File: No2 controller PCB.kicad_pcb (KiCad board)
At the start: 2 copper layers, 155 x 70 mm, 11 parts, among them SW1 SW_Push, SW2 SW_Push, U1 ProMicro

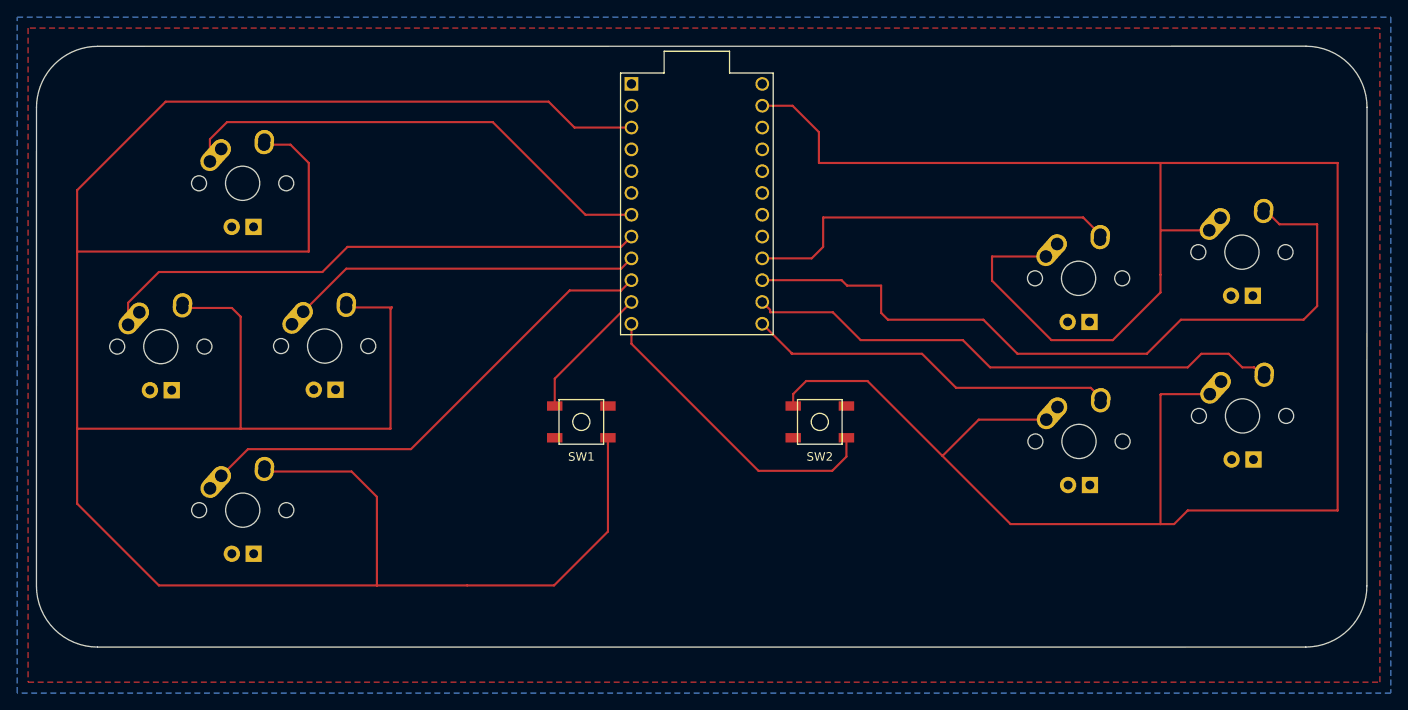
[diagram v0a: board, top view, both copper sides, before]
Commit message: added silkscreen, submitted to JLC
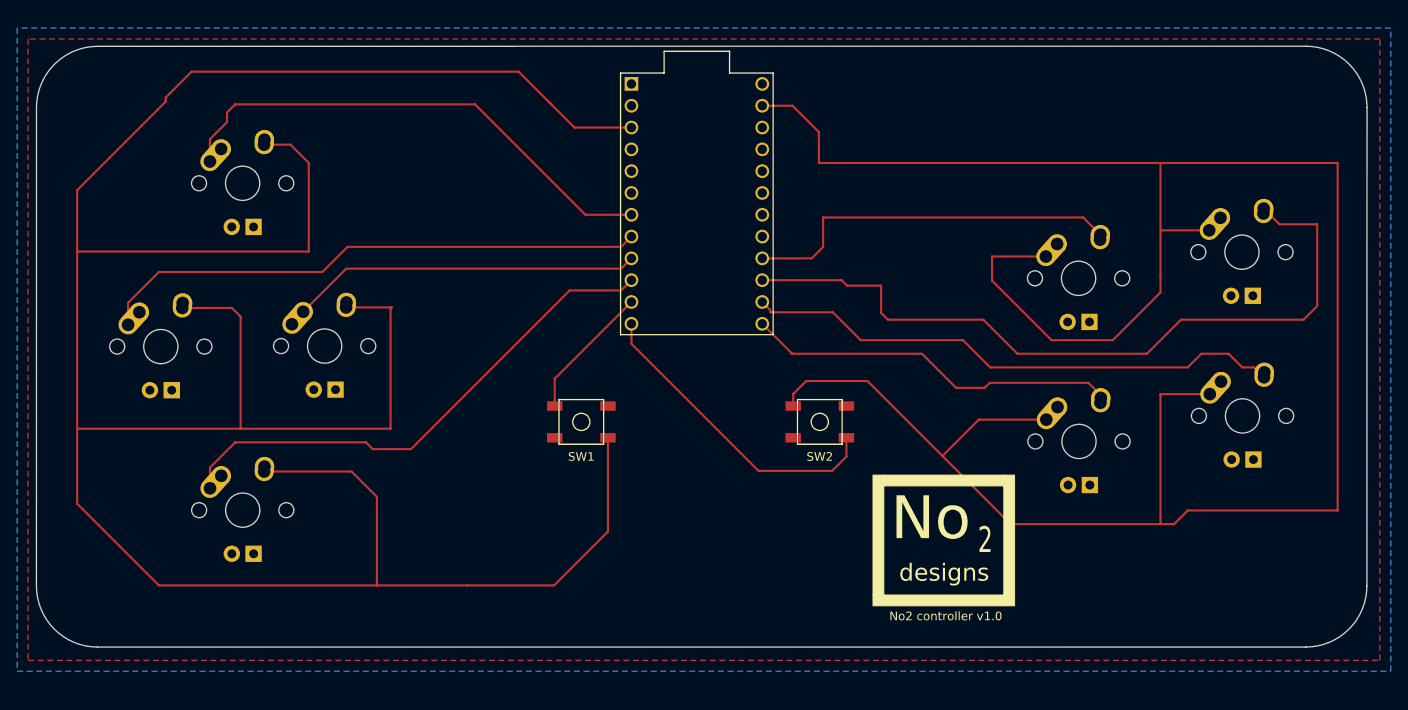
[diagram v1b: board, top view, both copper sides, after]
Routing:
- net Net-(MX3-Pad1): track 57.2 -> 61.2 mm
- net GND: track 605.2 -> 608.8 mm
- net Net-(MX6-Pad2): track 43.1 -> 45.6 mm
- net Net-(MX2-Pad1): track 57.0 -> 59.4 mm
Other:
- board text added: "2"
- board text added: "No"
- board text added: "No2 controller v1.0"
- board text added: "designs"
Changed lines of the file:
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@@
   (general
     (thickness 1.6)
-    (drawings 8)
-    (tracks 121)
+    (drawings 16)
+    (tracks 135)
     (zones 0)
     (modules 11)
@@
       (usegerberattributes false)
       (usegerberadvancedattributes false)
-      (creategerberjobfile false)
+      (creategerberjobfile true)
       (excludeedgelayer true)
       (linewidth 0.100000)
@@
       (net 22 GND))
   )
+  (gr_text "No2 controller v1.0\n" (at 166.601783 105.349946) (layer F.SilkS)
+    (effects (font (size 1 1) (thickness 0.15)))
+  )
+  (gr_poly (pts (xy 158.115 102.87) (xy 173.355 102.87) (xy 173.355 104.14) (xy 158.115 104.14)) (layer F.SilkS) (width 0.1))
+  (gr_poly (pts (xy 173.355 88.9) (xy 174.625 88.9) (xy 174.625 104.14) (xy 173.355 104.14)) (layer F.SilkS) (width 0.1))
+  (gr_poly (pts (xy 159.385 88.9) (xy 158.115 88.9) (xy 158.115 102.87) (xy 159.385 102.87)) (layer F.SilkS) (width 0.1))
+  (gr_poly (pts (xy 159.385 88.9) (xy 159.385 90.17) (xy 173.355 90.17) (xy 173.355 88.9)) (layer F.SilkS) (width 0.1))
+  (gr_text designs (at 166.408983 100.280101) (layer F.SilkS)
+    (effects (font (size 2 2) (thickness 0.15)))
+  )
+  (gr_text 2 (at 171.205497 96.475733) (layer F.SilkS)
+    (effects (font (size 3 2) (thickness 0.15)))
+  )
+  (gr_text No (at 164.855497 93.935733) (layer F.SilkS)
+    (effects (font (size 5 5) (thickness 0.15)))
+  )
   (gr_line (start 67.814594 38.956948) (end 208.550675 38.944895) (layer Edge.Cuts) (width 0.12))
   (gr_line (start 60.665993 101.830266) (end 60.670844 46.100698) (layer Edge.Cuts) (width 0.12))
@@
   (segment (start 71.344702 68.831548) (end 74.93 65.24625) (width 0.25) (layer F.Cu) (net 1))
   (segment (start 124.61875 58.57875) (end 129.979611 58.57875) (width 0.25) (layer F.Cu) (net 2))
-  (segment (start 113.82375 47.78375) (end 124.61875 58.57875) (width 0.25) (layer F.Cu) (net 2))
-  (segment (start 82.8675 47.78375) (end 113.82375 47.78375) (width 0.25) (layer F.Cu) (net 2))
+  (segment (start 80.875138 49.776112) (end 82.8675 47.78375) (width 0.25) (layer F.Cu) (net 2))
   (segment (start 80.875138 52.372158) (end 80.875138 49.776112) (width 0.25) (layer F.Cu) (net 2))
-  (segment (start 80.875138 49.776112) (end 82.8675 47.78375) (width 0.25) (layer F.Cu) (net 2))
+  (segment (start 82.8675 46.6725) (end 83.82 45.72) (width 0.25) (layer F.Cu) (net 2))
+  (segment (start 83.82 45.72) (end 111.76 45.72) (width 0.25) (layer F.Cu) (net 2))
+  (segment (start 82.8675 47.78375) (end 82.8675 46.6725) (width 0.25) (layer F.Cu) (net 2))
+  (segment (start 111.76 45.72) (end 124.61875 58.57875) (width 0.25) (layer F.Cu) (net 2))
   (segment (start 122.784607 67.397893) (end 104.29875 85.88375) (width 0.25) (layer F.Cu) (net 3))
-  (segment (start 85.304983 85.88375) (end 82.197762 88.990971) (width 0.25) (layer F.Cu) (net 3))
-  (segment (start 104.29875 85.88375) (end 85.304983 85.88375) (width 0.25) (layer F.Cu) (net 3))
   (segment (start 128.780468 67.397893) (end 129.979611 66.19875) (width 0.25) (layer F.Cu) (net 3))
   (segment (start 122.784607 67.397893) (end 128.780468 67.397893) (width 0.25) (layer F.Cu) (net 3))
+  (segment (start 80.887762 90.450971) (end 80.887762 88.022238) (width 0.25) (layer F.Cu) (net 3))
+  (segment (start 80.887762 88.022238) (end 83.82 85.09) (width 0.25) (layer F.Cu) (net 3))
+  (segment (start 83.82 85.09) (end 99.06 85.09) (width 0.25) (layer F.Cu) (net 3))
+  (segment (start 99.85375 85.88375) (end 104.29875 85.88375) (width 0.25) (layer F.Cu) (net 3))
+  (segment (start 99.06 85.09) (end 99.85375 85.88375) (width 0.25) (layer F.Cu) (net 3))
   (segment (start 128.780468 64.857893) (end 129.979611 63.65875) (width 0.25) (layer F.Cu) (net 4))
   (segment (start 91.740823 69.874165) (end 96.757095 64.857893) (width 0.25) (layer F.Cu) (net 4))
@@
   (segment (start 148.644338 74.77125) (end 163.83 74.77125) (width 0.25) (layer F.Cu) (net 6))
   (segment (start 163.83 74.77125) (end 167.79875 78.74) (width 0.25) (layer F.Cu) (net 6))
-  (segment (start 183.49321 78.74) (end 184.658491 79.905281) (width 0.25) (layer F.Cu) (net 6))
-  (segment (start 167.79875 78.74) (end 183.49321 78.74) (width 0.25) (layer F.Cu) (net 6))
   (segment (start 148.644338 74.703477) (end 145.219611 71.27875) (width 0.25) (layer F.Cu) (net 6))
   (segment (start 148.644338 74.77125) (end 148.644338 74.703477) (width 0.25) (layer F.Cu) (net 6))
+  (segment (start 184.618491 80.485281) (end 184.618491 79.208491) (width 0.25) (layer F.Cu) (net 6))
+  (segment (start 184.618491 80.485281) (end 184.618491 79.562981) (width 0.25) (layer F.Cu) (net 6))
+  (segment (start 184.618491 79.562981) (end 183.212794 78.157284) (width 0.25) (layer F.Cu) (net 6))
+  (segment (start 183.212794 78.157284) (end 171.7164 78.157284) (width 0.25) (layer F.Cu) (net 6))
+  (segment (start 171.133684 78.74) (end 167.79875 78.74) (width 0.25) (layer F.Cu) (net 6))
+  (segment (start 171.7164 78.157284) (end 171.133684 78.74) (width 0.25) (layer F.Cu) (net 6))
   (segment (start 205.474888 59.69) (end 203.639463 57.854575) (width 0.25) (layer F.Cu) (net 7))
   (segment (start 209.8675 59.69) (end 205.474888 59.69) (width 0.25) (layer F.Cu) (net 7))
@@
   (segment (start 127.2425 95.48375) (end 127.2425 85.165) (width 0.25) (layer F.Cu) (net 22))
   (segment (start 120.9675 101.75875) (end 127.2425 95.48375) (width 0.25) (layer F.Cu) (net 22))
-  (segment (start 123.34875 48.41875) (end 129.979611 48.41875) (width 0.25) (layer F.Cu) (net 22))
   (segment (start 120.3325 45.4025) (end 123.34875 48.41875) (width 0.25) (layer F.Cu) (net 22))
-  (segment (start 75.72375 45.4025) (end 120.3325 45.4025) (width 0.25) (layer F.Cu) (net 22))
   (segment (start 65.405 62.865) (end 65.405 55.72125) (width 0.25) (layer F.Cu) (net 22))
   (segment (start 65.405 55.72125) (end 75.72375 45.4025) (width 0.25) (layer F.Cu) (net 22))
@@
   (segment (start 191.61125 52.54625) (end 151.819338 52.54625) (width 0.25) (layer F.Cu) (net 22))
   (segment (start 151.819338 52.54625) (end 151.819338 48.949338) (width 0.25) (layer F.Cu) (net 22))
+  (segment (start 75.72375 45.4025) (end 75.72375 44.92625) (width 0.25) (layer F.Cu) (net 22))
+  (segment (start 75.72375 44.92625) (end 76.2 44.45) (width 0.25) (layer F.Cu) (net 22))
+  (segment (start 119.38 44.45) (end 120.65 45.72) (width 0.25) (layer F.Cu) (net 22))
+  (segment (start 76.2 44.45) (end 78.74 41.91) (width 0.25) (layer F.Cu) (net 22))
+  (segment (start 78.74 41.91) (end 116.84 41.91) (width 0.25) (layer F.Cu) (net 22))
+  (segment (start 116.84 41.91) (end 119.38 44.45) (width 0.25) (layer F.Cu) (net 22))
+  (segment (start 123.34875 48.41875) (end 129.979611 48.41875) (width 0.25) (layer F.Cu) (net 22))
   (zone (net 22) (net_name GND) (layer F.Cu) (hatch edge 0.508)
     (connect_pads (clearance 0.508))
@@
     (polygon
       (pts
-        (xy 217.17 36.83) (xy 59.69 36.83) (xy 59.69 113.03) (xy 217.17 113.03)
+        (xy 217.17 38.1) (xy 59.69 38.1) (xy 59.69 110.49) (xy 217.17 110.49)
       )
     )
@@
     (polygon
       (pts
-        (xy 58.42 35.56) (xy 218.44 35.56) (xy 218.44 114.3) (xy 58.42 114.3)
+        (xy 218.44 36.83) (xy 58.42 36.83) (xy 58.42 111.76) (xy 218.44 111.76)
       )
     )
